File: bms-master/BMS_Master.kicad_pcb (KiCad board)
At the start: 2 copper layers, 65 x 45 mm, 94 parts, among them J1 Conn_PWR, J2 PROG, J3 Conn_Fault, J4 BMS_M_IN, J5 Conn_CAN, J6 Conn_CSR, J7 Conn_CSROUT, J8 Micro_SD_Card, SW1 SW_SPST, U1 AP2204K-ADJ, U2 AP2204K-ADJ, U3 STM32F103C8Tx, U4 BQ79600-Q1, U5 SN65HVD256D, U6 TLV2371DBV, U7 TLV2371DBV, Y1 8M, Y2 32.768k

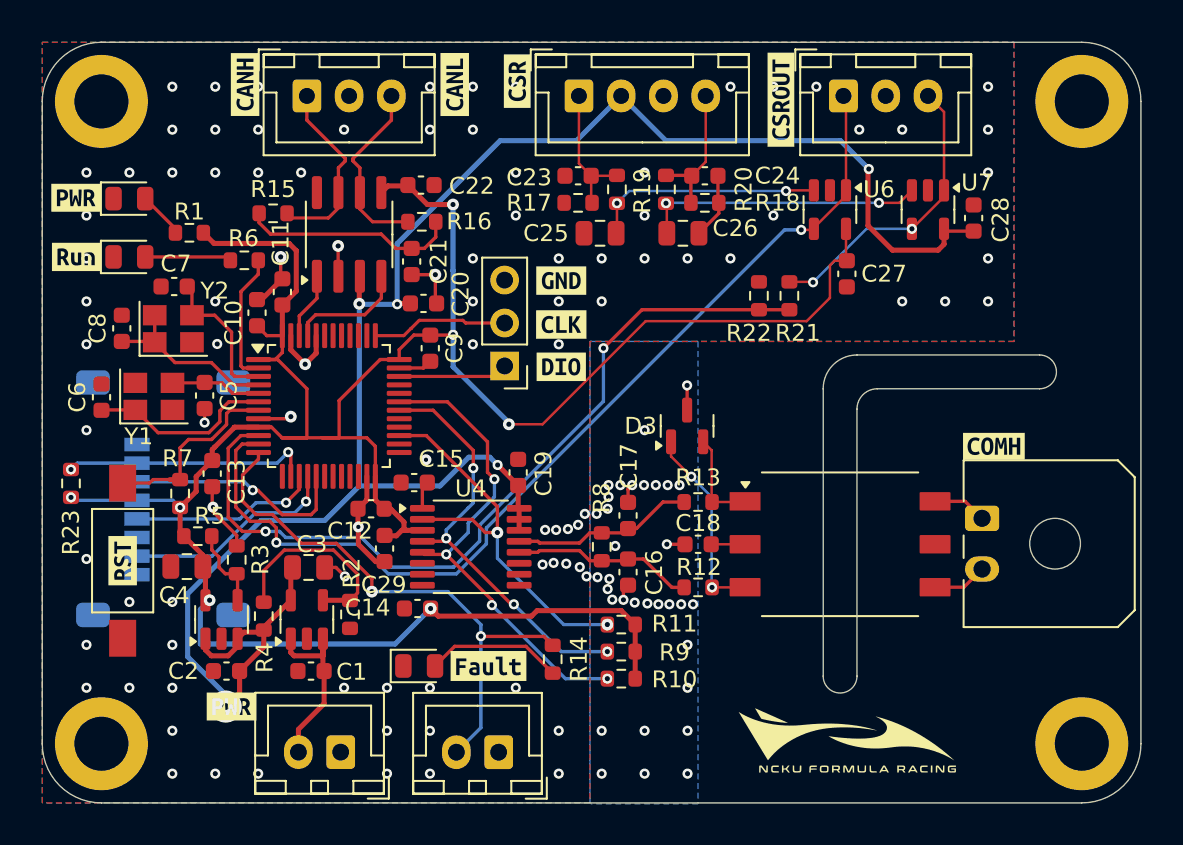
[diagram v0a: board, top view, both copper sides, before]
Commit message: feat: wireless BMS and USB power
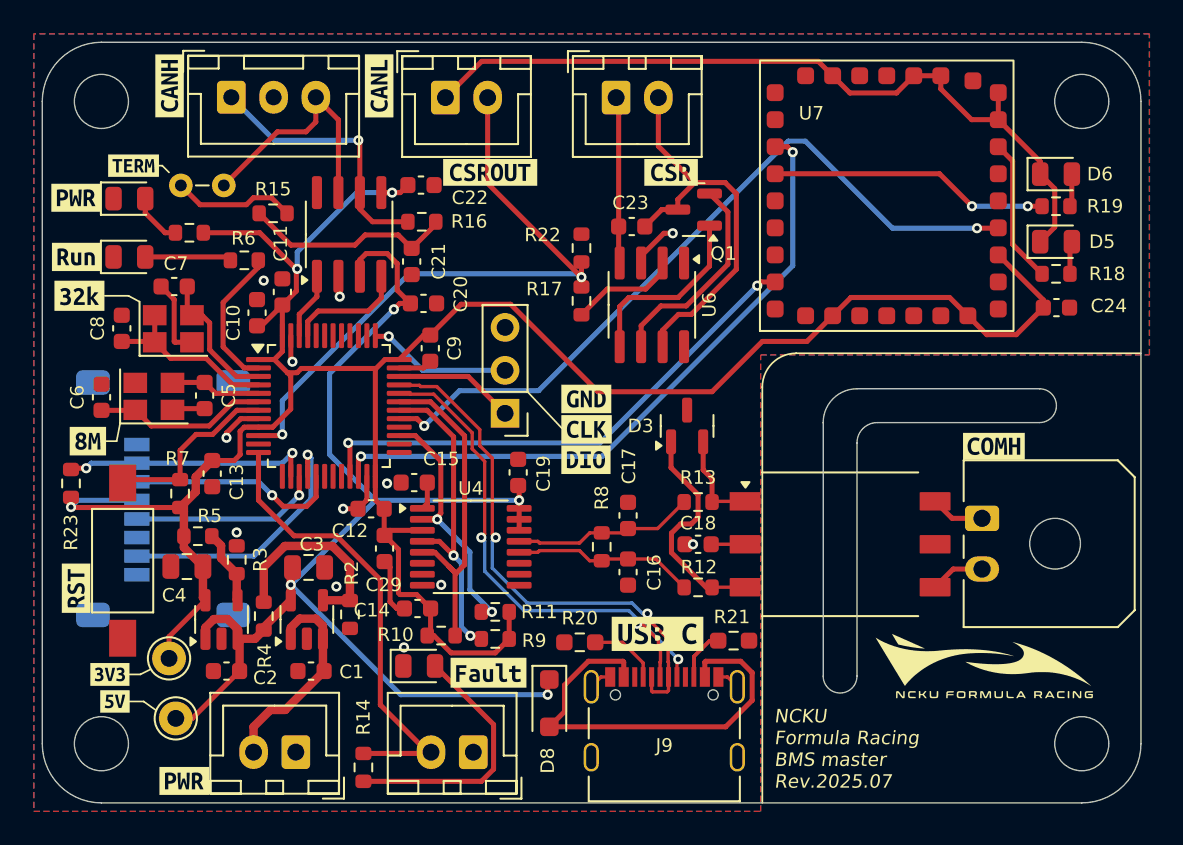
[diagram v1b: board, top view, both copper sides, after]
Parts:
- removed C25, C26: 220n, Capacitor_SMD:C_0805_2012Metric
- removed C27, C28: 100n, Capacitor_SMD:C_0603_1608Metric
- removed kibuzzard-67D6BCA3: G***, kibuzzard-67D6BCA3
- added D5: LED2, LED_SMD:LED_0805_2012Metric, F.Cu at (125.5, 53.3)
- added D6: LED1, LED_SMD:LED_0805_2012Metric, F.Cu at (125.5, 49.3)
- added D8: MBR230SFT, Diode_SMD:D_SOD-123F, F.Cu at (95.5, 80.6)
- added J9: USB_C_Receptacle_USB2.0_16P, Connector_USB:USB_C_Receptacle_Palconn_UTC16-G, F.Cu at (102.3, 81.6)
- added JP1: Jumper_2_Open, PCM_Jumper_AKL:Jumper_P2.54mm_D0.7mm, F.Cu at (76.2, 50.0)
- added Q1: SS9013, Package_TO_SOT_SMD:SOT-23, F.Cu at (104.0, 51.4)
- added TP1: TP_3V3, Connector_Pin:Pin_D1.0mm_L10.0mm, F.Cu at (73.0, 78.0)
- added TP2: TP_5V, Connector_Pin:Pin_D1.0mm_L10.0mm, F.Cu at (73.4, 81.5)
- added kibuzzard-68838A70: G***, kibuzzard-68838A70, F.Cu at (101.9, 76.5)
- added kibuzzard-68838B00: G***, kibuzzard-68838B00, F.Cu at (67.7, 56.5)
- added kibuzzard-68838B09: G***, kibuzzard-68838B09, F.Cu at (68.2, 65.1)
- added kibuzzard-68838DBE: G***, kibuzzard-68838DBE, F.Cu at (69.5, 78.9)
- added kibuzzard-68838DC4: G***, kibuzzard-68838DC4, F.Cu at (69.8, 80.5)
- added kibuzzard-68838E18: G***, kibuzzard-68838E18, F.Cu at (70.9, 48.8)
- C23: value 100n -> 10n
- H1, H2, H3, H4: value MountingHole_Pad -> MountingHole; footprint MountingHole:MountingHole_3.2mm_M3_ISO14580_Pad -> MountingHole:MountingHole_3.2mm_M3_DIN965
- J6: value Conn_CSR -> Conn_CRSOUT; footprint Connector_JST:JST_XH_B4B-XH-A_1x04_P2.50mm_Vertical -> Connector_JST:JST_XH_B2B-XH-A_1x02_P2.50mm_Vertical
- J7: value Conn_CSROUT -> Conn_CRS; footprint Connector_JST:JST_XH_B3B-XH-A_1x03_P2.50mm_Vertical -> Connector_JST:JST_XH_B2B-XH-A_1x02_P2.50mm_Vertical
- R17: value 10K -> 11.25k
- R18, R19: value 10K -> 1k
- R20: value 10K -> 5k1; footprint Resistor_SMD:R_0603_1608Metric -> Resistor_SMD:R_0603_1608Metric_Pad0.98x0.95mm_HandSolder
- R21: value 100k -> 5k1; footprint Resistor_SMD:R_0603_1608Metric -> Resistor_SMD:R_0603_1608Metric_Pad0.98x0.95mm_HandSolder
- R22: value 200k -> 30R
- U6: value TLV2371DBV -> XTR117; footprint Package_TO_SOT_SMD:SOT-23-5 -> Package_SO:SOIC-8_3.9x4.9mm_P1.27mm
- U7: value TLV2371DBV -> ~; footprint Package_TO_SOT_SMD:SOT-23-5 -> Daphnis-I:Daphnis-I
- moved R20 27.3 mm to (97.3, 77.0), turned to 0 degrees
- moved R19 26.0 mm to (125.5, 51.2), turned to 0 degrees
- moved J7 23.6 mm to (89.3, 44.8)
- moved C24 22.2 mm to (125.5, 57.2)
- moved R18 21.2 mm to (125.5, 55.2)
- moved R21 20.7 mm to (106.4, 76.9), turned to 180 degrees
- moved kibuzzard-67C3D9C1 17.7 mm to (92.0, 49.2), turned to 0 degrees
- moved R14 12.9 mm to (84.5, 84.4)
- moved U7 12.3 mm to (108.0, 58.6), turned to 90 degrees
- moved U6 11.9 mm to (101.6, 57.0)
- moved R10 11.0 mm to (89.1, 76.6), turned to 0 degrees
- moved R22 10.9 mm to (97.4, 53.7)
- moved kibuzzard-67C3D8F9 10.6 mm to (102.7, 49.2), turned to 0 degrees
- moved G*** 9.22 mm to (121.3, 78.4)
- moved R11 7.49 mm to (92.3, 75.2)
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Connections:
- C23 pad 1: Net-(J6-Pin_1) -> Net-(J6-Pin_2)
- C23 pad 2: GND -> Net-(J6-Pin_1)
- C24 pad 1: Net-(J6-Pin_4) -> VIO
- J5 pad 1: CAN_P -> CAN_N
- J5 pad 3: CAN_N -> CAN_P
- J6 pad 2: +5V -> Net-(J6-Pin_2)
- J7 pad 1: CRS2 -> GND
- J7 pad 2: GND -> CRS
- R15 pad 2: CAN_P -> Net-(JP1-B)
- R17 pad 1: Net-(J6-Pin_1) -> CRS
- R17 pad 2: GND -> Net-(U6-IIN)
- R18 pad 1: Net-(J6-Pin_4) -> Net-(U7-LED2)
- R18 pad 2: GND -> Net-(D5-A)
- R19 pad 1: Net-(U6-+) -> Net-(U7-LED1)
- R19 pad 2: Net-(J6-Pin_1) -> Net-(D6-A)
- R20 pad 1: Net-(U7-+) -> GND
- R20 pad 2: Net-(J6-Pin_4) -> Net-(J9-CC1)
- R21 pad 1: CRS1 -> GND
- R21 pad 2: CRS1_DIV -> Net-(J9-CC2)
- R22 pad 1: CRS1_DIV -> CRS
- U3 pad 10: CRS1_DIV -> CRS
- U3 pad 11: CRS2 -> unconnected-(U3-PA1-Pad11)
- U3 pad 21: unconnected-(U3-PB10-Pad21) -> LoRa_TX
- U3 pad 22: unconnected-(U3-PB11-Pad22) -> LoRa_RX
- U3 pad 29: unconnected-(U3-PA8-Pad29) -> LoRa_RST
- U3 pad 32: unconnected-(U3-PA11-Pad32) -> USB_D+
- U3 pad 33: unconnected-(U3-PA12-Pad33) -> USB_D-
- U6 pad 1: CRS2 -> unconnected-(U6-VREF-Pad1)
- U6 pad 2: GND -> Net-(U6-IIN)
- U6 pad 3: Net-(U6-+) -> GND
- U6 pad 4: CRS2 -> Net-(J6-Pin_1)
- U6 pad 5: VIO -> Net-(Q1-E)
- U7 pad 1: CRS1 -> unconnected-(U7-GPIO_0-Pad1)
- U7 pad 2: GND -> unconnected-(U7-GPIO_1-Pad2)
- U7 pad 3: Net-(U7-+) -> VIO
- U7 pad 4: CRS1 -> LoRa_RST
- U7 pad 5: +5V -> unconnected-(U7-LPUTXD1-Pad5)
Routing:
- net CRS2: track 58.9 -> 0.00 mm, vias 2 -> 0
- net CRS1_DIV: track 49.3 -> 0.00 mm, vias 2 -> 0
- net LoRa_RST: track 0.00 -> 44.7 mm, vias 0 -> 2
- net LoRa_RX: track 0.00 -> 39.4 mm, vias 0 -> 2
- net CRS: track 0.00 -> 38.7 mm, vias 0 -> 2
- net +5V: track 112.8 -> 75.1 mm, vias 5 -> 4
- net GND: track 37.7 -> 73.4 mm, vias 128 -> 12
- net USB_D+: track 0.00 -> 32.7 mm, vias 0 -> 3
- net USB_D-: track 0.00 -> 31.8 mm, vias 0 -> 2
- net LoRa_TX: track 0.00 -> 31.2 mm, vias 0 -> 2
- net Net-(D8-A): track 0.00 -> 26.1 mm
- net Net-(J6-Pin_2): track 0.00 -> 24.3 mm
- net CRS1: track 17.6 -> 0.00 mm, vias 2 -> 0
- net Net-(U7-+): track 17.1 -> 0.00 mm, vias 2 -> 0
- net Net-(U7-LED1): track 0.00 -> 16.6 mm, vias 0 -> 2
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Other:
- outline, holes or cut-outs redrawn
- board text added: "NCKU Formula Racing BMS master Rev.2025.07"

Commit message: fix: USB and USART traces
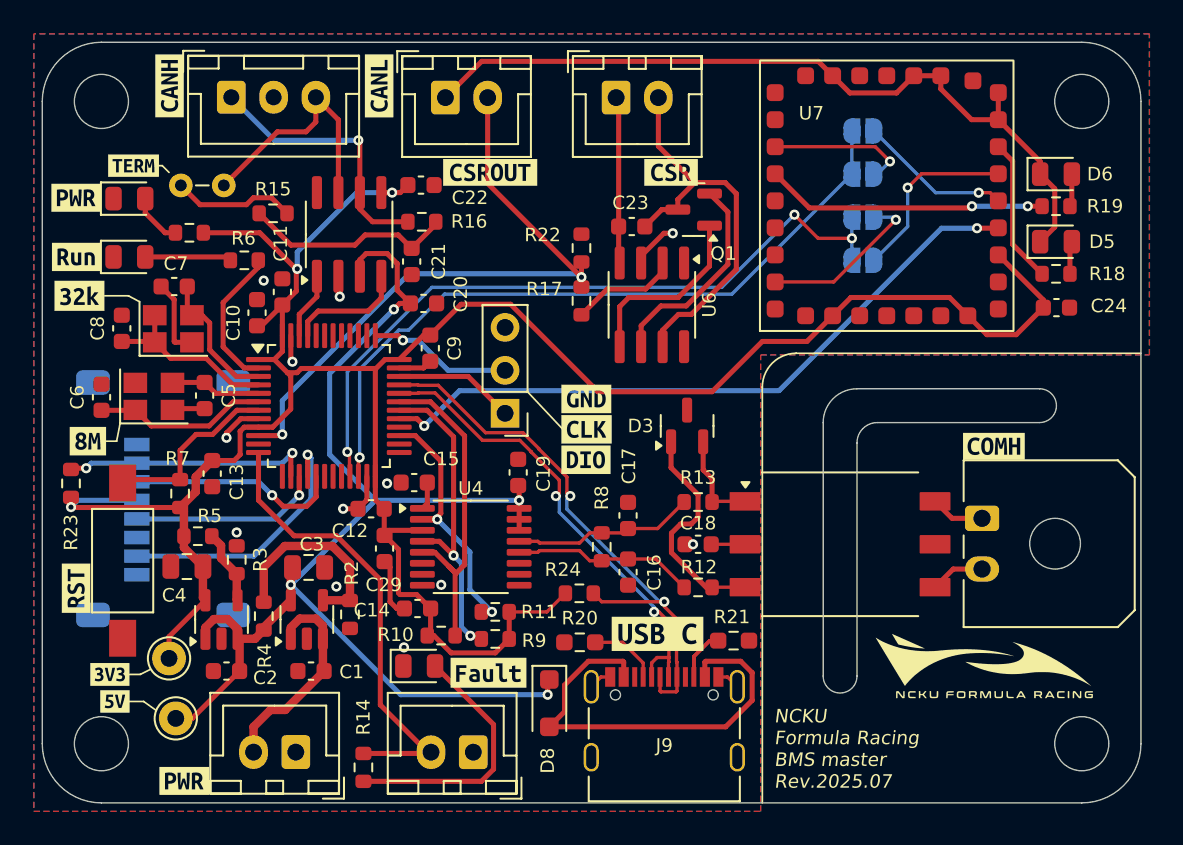
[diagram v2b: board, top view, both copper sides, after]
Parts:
- added JP2: LPUTX, Jumper:SolderJumper-2_P1.3mm_Open_RoundedPad1.0x1.5mm, B.Cu at (114.0, 46.8)
- added JP3: UTX, Jumper:SolderJumper-2_P1.3mm_Open_RoundedPad1.0x1.5mm, B.Cu at (114.0, 49.3)
- added JP4: URX, Jumper:SolderJumper-2_P1.3mm_Open_RoundedPad1.0x1.5mm, B.Cu at (114.0, 51.9)
- added JP5: LPURX, Jumper:SolderJumper-2_P1.3mm_Open_RoundedPad1.0x1.5mm, B.Cu at (114.0, 54.4)
- added R24: 1k5, Resistor_SMD:R_0603_1608Metric, F.Cu at (97.3, 74.1)
- added kibuzzard-68BABEC4: G***, kibuzzard-68BABEC4, B.Cu at (118.2, 46.8)
- added kibuzzard-68BABEE5: G***, kibuzzard-68BABEE5, B.Cu at (117.4, 49.3)
- added kibuzzard-68BABEF1: G***, kibuzzard-68BABEF1, B.Cu at (118.2, 54.4)
- added kibuzzard-68BABF14: G***, kibuzzard-68BABF14, B.Cu at (117.4, 51.9)
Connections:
- U3 pad 32: USB_D+ -> USB_D-
- U3 pad 33: USB_D- -> USB_D+
- U7 pad 19: LoRa_RX -> Net-(JP3-A)
- U7 pad 24: LoRa_TX -> Net-(JP4-A)
- U7 pad 5: unconnected-(U7-LPUTXD1-Pad5) -> Net-(JP2-A)
- U7 pad 6: unconnected-(U7-LPURXD1-Pad6) -> Net-(JP5-A)
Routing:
- net LoRa_TX: track 31.2 -> 43.1 mm, vias 2 -> 3
- net Net-(JP5-A): track 0.00 -> 10.8 mm, vias 0 -> 1
- net Net-(JP4-A): track 0.00 -> 10.0 mm, vias 0 -> 1
- net Net-(JP2-A): track 0.00 -> 9.07 mm, vias 0 -> 1
- net Net-(JP3-A): track 0.00 -> 8.41 mm, vias 0 -> 1
- net LoRa_RST: track 44.7 -> 40.5 mm
- net VIO: track 144.9 -> 148.7 mm
- net USB_D-: track 31.8 -> 28.3 mm
- net LoRa_RX: track 39.4 -> 42.8 mm, vias 2 -> 1
- net USB_D+: track 32.7 -> 34.2 mm, vias 3 -> 2

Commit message: fix: CAN bus pin error
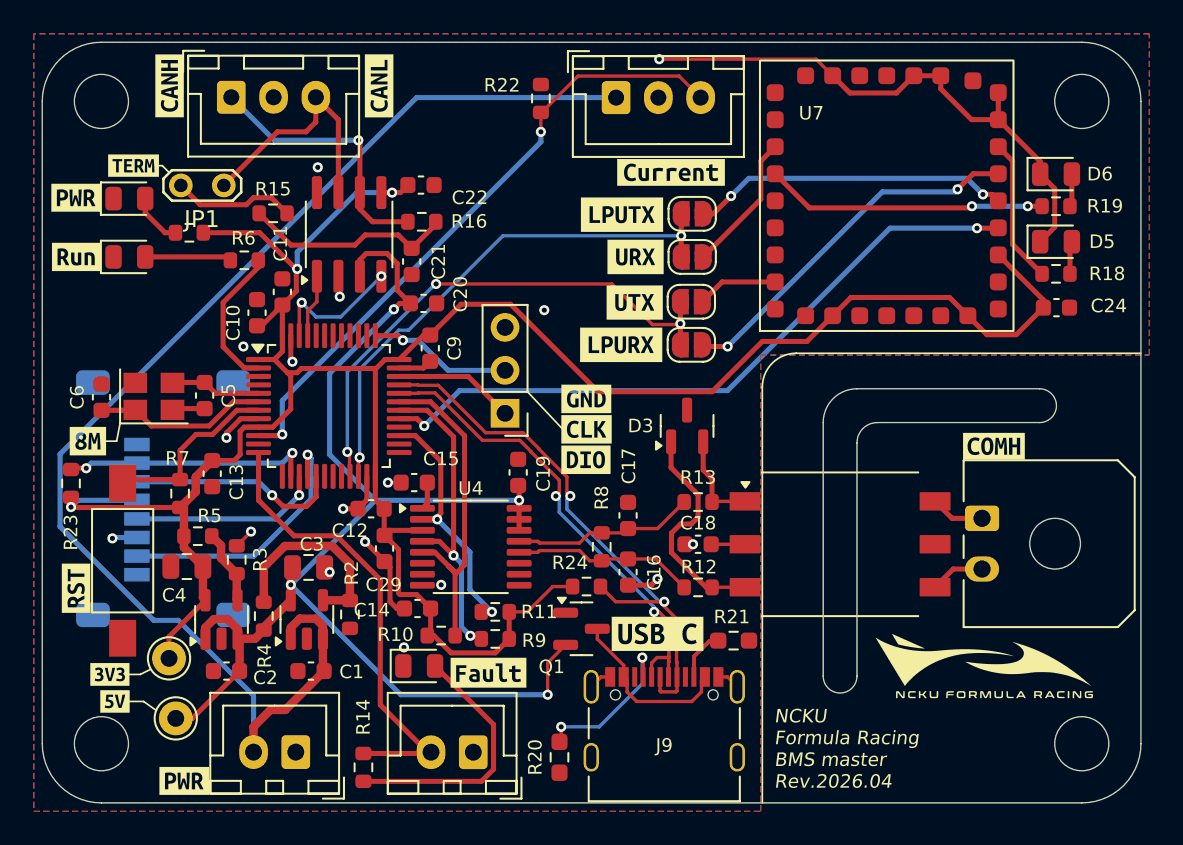
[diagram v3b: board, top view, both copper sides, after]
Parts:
- removed C23: 10n, Capacitor_SMD:C_0603_1608Metric
- removed C7, C8: 20p, Capacitor_SMD:C_0603_1608Metric
- removed D8: MBR230SFT, Diode_SMD:D_SOD-123F
- removed J7: Conn_CRS, Connector_JST:JST_XH_B2B-XH-A_1x02_P2.50mm_Vertical
- removed R17: 11.25k, Resistor_SMD:R_0603_1608Metric
- removed U6: XTR117, Package_SO:SOIC-8_3.9x4.9mm_P1.27mm
- removed Y2: 32.768k, Crystal:Crystal_SMD_SeikoEpson_FA238-4Pin_3.2x2.5mm
- removed kibuzzard-67C3D8F9: G***, kibuzzard-67C3D8F9
- removed kibuzzard-67C3D9C1: G***, kibuzzard-67C3D9C1
- removed kibuzzard-68838B00: G***, kibuzzard-68838B00
- added kibuzzard-69EA7393: G***, kibuzzard-69EA7393, F.Cu at (102.7, 49.2)
- J6: value Conn_CRSOUT -> Conn_CRS; footprint Connector_JST:JST_XH_B2B-XH-A_1x02_P2.50mm_Vertical -> Connector_JST:JST_XH_B3B-XH-A_1x03_P2.50mm_Vertical
- JP1: footprint PCM_Jumper_AKL:Jumper_P2.54mm_D0.7mm -> TestPoint:TestPoint_2Pads_Pitch2.54mm_Drill0.8mm
- JP2, JP3, JP4, JP5, kibuzzard-68BABEC4, kibuzzard-68BABEE5, kibuzzard-68BABEF1, kibuzzard-68BABF14: moved to F.Cu
- Q1: value SS9013 -> 2N7002
- moved Q1 25.7 mm to (97.4, 76.2), turned to 0 degrees
- moved kibuzzard-68BABEF1 19.1 mm to (99.8, 59.4), turned to 0 degrees
- moved kibuzzard-68BABEC4 19.0 mm to (99.8, 51.7), turned to 0 degrees
- moved kibuzzard-68BABF14 17.6 mm to (100.5, 56.9), turned to 0 degrees
- moved kibuzzard-68BABEE5 17.5 mm to (100.6, 54.2), turned to 0 degrees
- moved JP4 11.3 mm to (103.9, 56.9)
- moved JP5 11.3 mm to (103.9, 59.4)
- moved JP3 11.2 mm to (104.0, 54.2)
- moved JP2 11.2 mm to (104.0, 51.6)
- moved R22 9.17 mm to (95.0, 44.8)
- moved R20 6.91 mm to (96.1, 83.8), turned to 90 degrees
- moved R24 0.58 mm to (97.7, 73.7)
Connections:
- J6 pad 1: Net-(J6-Pin_1) -> +24V
- J6 pad 2: Net-(J6-Pin_2) -> GND
- J9 pad A4: Net-(D8-A) -> Net-(Q1-D)
- J9 pad A9: Net-(D8-A) -> Net-(Q1-D)
- J9 pad B4: Net-(D8-A) -> Net-(Q1-D)
- J9 pad B9: Net-(D8-A) -> Net-(Q1-D)
- Q1 pad 1: Net-(Q1-E) -> GND
- Q1 pad 2: Net-(Q1-B) -> +5V
- Q1 pad 3: Net-(J6-Pin_2) -> Net-(Q1-D)
- U3 pad 3: /LSE_IN -> unconnected-(U3-PC14-Pad3)
- U3 pad 4: /LSE_OUT -> unconnected-(U3-PC15-Pad4)
- U3 pad 45: CAN_RX -> CAN_TX
- U3 pad 46: CAN_TX -> CAN_RX
- U5 pad 8: unconnected-(U5-S-Pad8) -> GND
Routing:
- net +24V: track 12.7 -> 77.6 mm
- net Net-(D8-A): track 26.1 -> 0.00 mm
- net Net-(J6-Pin_2): track 24.3 -> 0.00 mm
- net GND: track 73.4 -> 59.8 mm, vias 12 -> 17
- net Net-(Q1-B): track 12.5 -> 0.00 mm
- net LoRa_RX: track 42.8 -> 31.2 mm, vias 1 -> 2
- net LoRa_TX: track 43.1 -> 31.7 mm
- net Net-(Q1-E): track 11.1 -> 0.00 mm
- net Net-(JP5-A): track 10.8 -> 21.8 mm, vias 1 -> 2
- net /LSE_OUT: track 10.8 -> 0.00 mm
- net Net-(Q1-D): track 0.00 -> 10.3 mm
- net Net-(J6-Pin_1): track 9.87 -> 0.00 mm
- net Net-(JP2-A): track 9.07 -> 18.9 mm, vias 1 -> 2
- net /LSE_IN: track 8.18 -> 0.00 mm
- net Net-(U6-IIN): track 6.39 -> 0.00 mm
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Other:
- board text added: "NCKU Formula Racing BMS master Rev.2026.04"
- board text removed: "NCKU Formula Racing BMS master Rev.2025.07"

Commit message: feat: add DCDC and fix layout
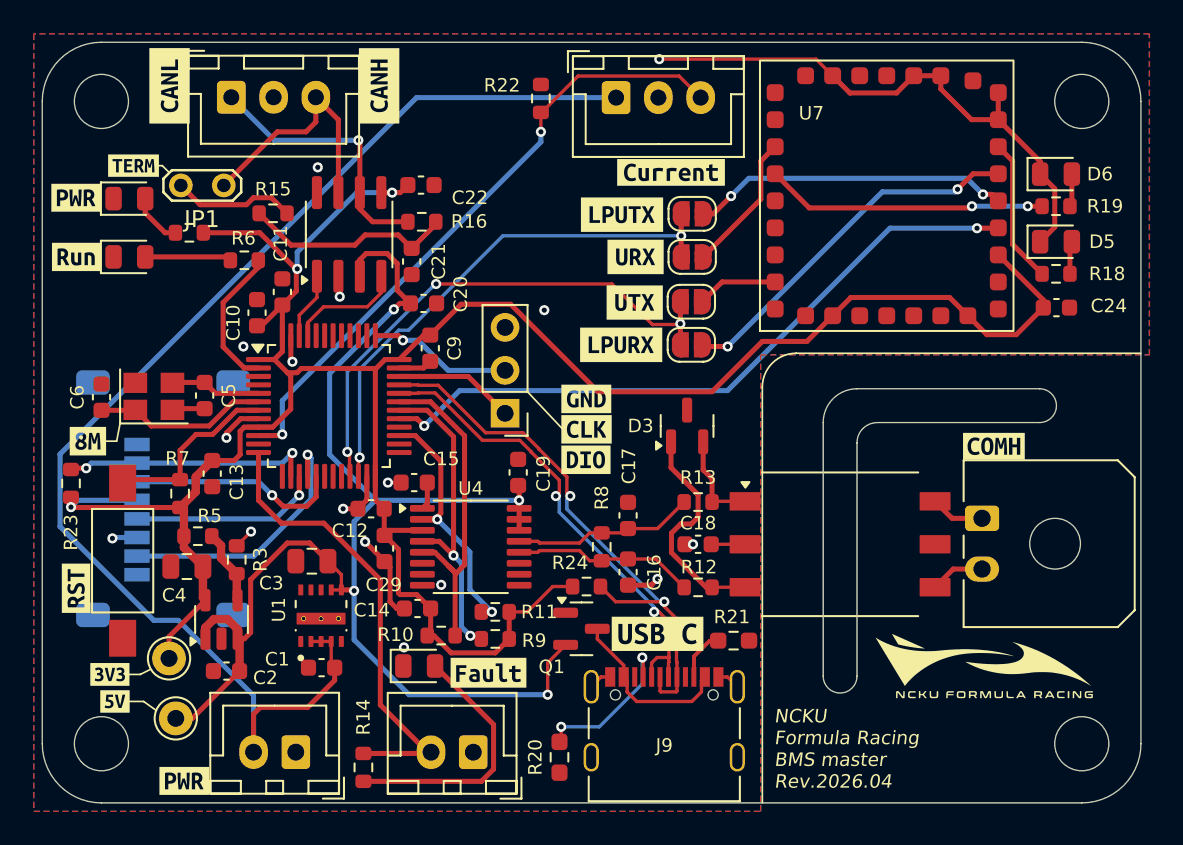
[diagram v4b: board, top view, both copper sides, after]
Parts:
- removed R2: 100k, Resistor_SMD:R_0603_1608Metric
- removed R4: 301k, Resistor_SMD:R_0603_1608Metric
- removed kibuzzard-679F55A0: G***, kibuzzard-679F55A0
- removed kibuzzard-679F55DD: G***, kibuzzard-679F55DD
- added kibuzzard-69EB13FF: G***, kibuzzard-69EB13FF, F.Cu at (85.4, 44.1)
- added kibuzzard-69EB1406: G***, kibuzzard-69EB1406, F.Cu at (73.0, 44.1)
- U1: value AP2204K-ADJ -> LMZM23600V5SILR; footprint Package_TO_SOT_SMD:SOT-23-5 -> bms-master:MODULE_LMZM23601V5SILR
- moved U1 0.87 mm to (82.0, 75.4)
- moved C1 0.66 mm to (82.0, 78.5)
- moved C3 0.42 mm to (81.5, 72.2), turned to 0 degrees
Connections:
- U1 pad 1: +24V -> GND
- U1 pad 2: GND -> +24V
- U1 pad 4: Net-(U1-ADJ) -> +24V
- U1 pad 5: +5V -> unconnected-(U1-PGOOD-Pad5)
- U3 pad 45: CAN_TX -> CAN_RX
- U3 pad 46: CAN_RX -> CAN_TX
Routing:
- net Net-(U1-ADJ): track 11.9 -> 0.00 mm
- net +5V: track 77.6 -> 81.4 mm
- net CAN_RX: track 8.08 -> 6.83 mm, vias 2 -> 0
- net +24V: track 77.6 -> 76.3 mm
- net GND: track 59.8 -> 59.4 mm, vias 17 -> 16
